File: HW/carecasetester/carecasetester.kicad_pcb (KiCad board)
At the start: 2 copper layers, 158.3 x 160.4 mm, 71 parts, among them J1 Conn_01x16_Female, J10-TP22 Conn_01x01_Male, J11-TP7 Conn_01x01_Male, J12-TP14 Conn_01x01_Male, J13-TP23 Conn_01x01_Male, J14-TP17 Conn_01x01_Male, J15 Conn_01x16_Male, J15-TP1 Conn_01x01_Male, J15-TP20 Conn_01x01_Male, J16-TP2 Conn_01x01_Male, J16-TP24 Conn_01x01_Male, J17-TP3 Conn_01x01_Male, J18-TP4 Conn_01x01_Male, J19-TP6 Conn_01x01_Male, J2 Conn_01x16_Female, J20-TP9 Conn_01x01_Male, J21-TP10 Conn_01x01_Male, J22-TP11 Conn_01x01_Male, J23-TP12 Conn_01x01_Male, J24-TP15 Conn_01x01_Male, J25-TP18 Conn_01x01_Male, J26-TP5 Conn_01x01_Male, J27-TP26 Conn_01x01_Male, J3 Conn_01x04_Female, J4 Conn_01x06_Male, J4-TP16 Conn_01x01_Male, J5 12V_Psu, J5-TP8 Conn_01x01_Male, J5-~E1 Conn_01x02_Male, J6-TP21 Conn_01x01_Male, J7-TP27 Conn_01x01_Male, J8-TP13 Conn_01x01_Male, J9-TP19 Conn_01x01_Male, K1 AZ952, Q1 BC847, SW1 SW_DIP_x02, U1 CD74HC4067M, U2 L7805

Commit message: missing schematic. (went poof)
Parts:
- added PulldownKnap: 4k7, Resistor_SMD:R_0603_1608Metric_Pad1.05x0.95mm_HandSolder, F.Cu at (208.8, 31.8)
- C1, C3: footprint Capacitor_SMD:C_0603_1608Metric_Pad1.05x0.95mm_HandSolder -> Capacitor_SMD:CP_Elec_6.3x5.4
- J5: moved to B.Cu
- moved R1 38.1 mm to (128.3, 47.4)
- moved J1 38.1 mm to (128.3, 52.3), turned to 270 degrees
- moved J2 38.1 mm to (167.3, 52.3), turned to 90 degrees
- moved D1 33.1 mm to (213.8, 54.0), turned to 90 degrees
- moved C1 19.1 mm to (157.0, 29.8), turned to 180 degrees
- moved C2 10.6 mm to (169.1, 33.0), turned to 180 degrees
- moved C3 9.85 mm to (181.7, 31.6), turned to 0 degrees
- turned J5 to 0 degrees
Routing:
- net Net-(J1-Pad3): track 189.6 -> 48.4 mm, vias 1 -> 0
- net Net-(J1-Pad4): track 185.5 -> 52.5 mm, vias 1 -> 0
- net Net-(J1-Pad5): track 180.3 -> 58.0 mm, vias 1 -> 0
- net Net-(J1-Pad6): track 175.7 -> 63.4 mm, vias 1 -> 0
- net Net-(J1-Pad7): track 171.0 -> 68.9 mm, vias 1 -> 0
- net Net-(J1-Pad8): track 163.7 -> 74.3 mm, vias 1 -> 0
- net Net-(J1-Pad9): track 157.5 -> 79.8 mm, vias 1 -> 0
- net Net-(J1-Pad10): track 151.5 -> 85.8 mm, vias 1 -> 0
- net Net-(J1-Pad11): track 143.3 -> 90.7 mm, vias 1 -> 0
- net Net-(D1-Pad1): track 157.8 -> 201.7 mm, vias 2 -> 4
- net Net-(J1-Pad12): track 138.4 -> 96.2 mm, vias 1 -> 0
- net Net-(J1-Pad13): track 129.5 -> 101.6 mm, vias 1 -> 0
- net Net-(J15-Pad6): track 140.5 -> 117.4 mm
- net Net-(J1-Pad14): track 122.0 -> 107.1 mm, vias 1 -> 0
- net Net-(J15-Pad10): track 119.7 -> 110.8 mm, vias 1 -> 3
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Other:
- outline, holes or cut-outs redrawn
- board text added: "1 2 3 4 5 6 7 8 9 10 11 12 13 14 15 16"
- board text added: "14 13 12 11 10 9 8 7 6 5 4 3 2 1 15 16"
- board text added: "C1+C2 footprints ændret til cp_elec 6.3-5.4 pulldown_knap tilføjet (47k resistor) byt ben i schematic på 12v stik (texas stik) Lav relay sheetet med Q1, R27 + D2"
- board text added: "Flip display headder"
- board text added: "GND TP1 TP2 TP3 TP4 TP6 TP9 TP10 TP11 TP12 TP15 TP18 TP5 TP26 GND GND"
- board text added: "SCL SDA +5V GND"

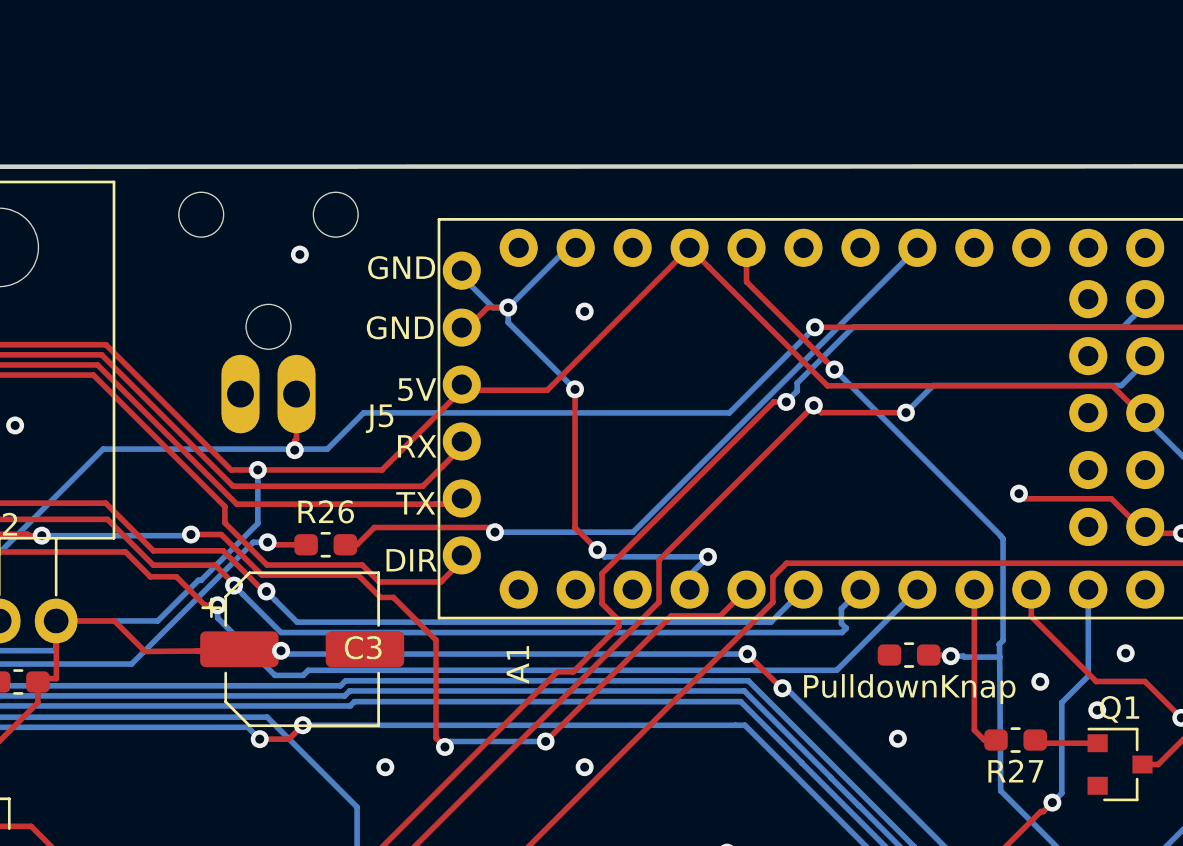
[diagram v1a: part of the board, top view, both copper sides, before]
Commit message: First try to fit schematic to pcb (not imported footprints to pcb yet)
Schematic: All known components has gotten an updated footprint
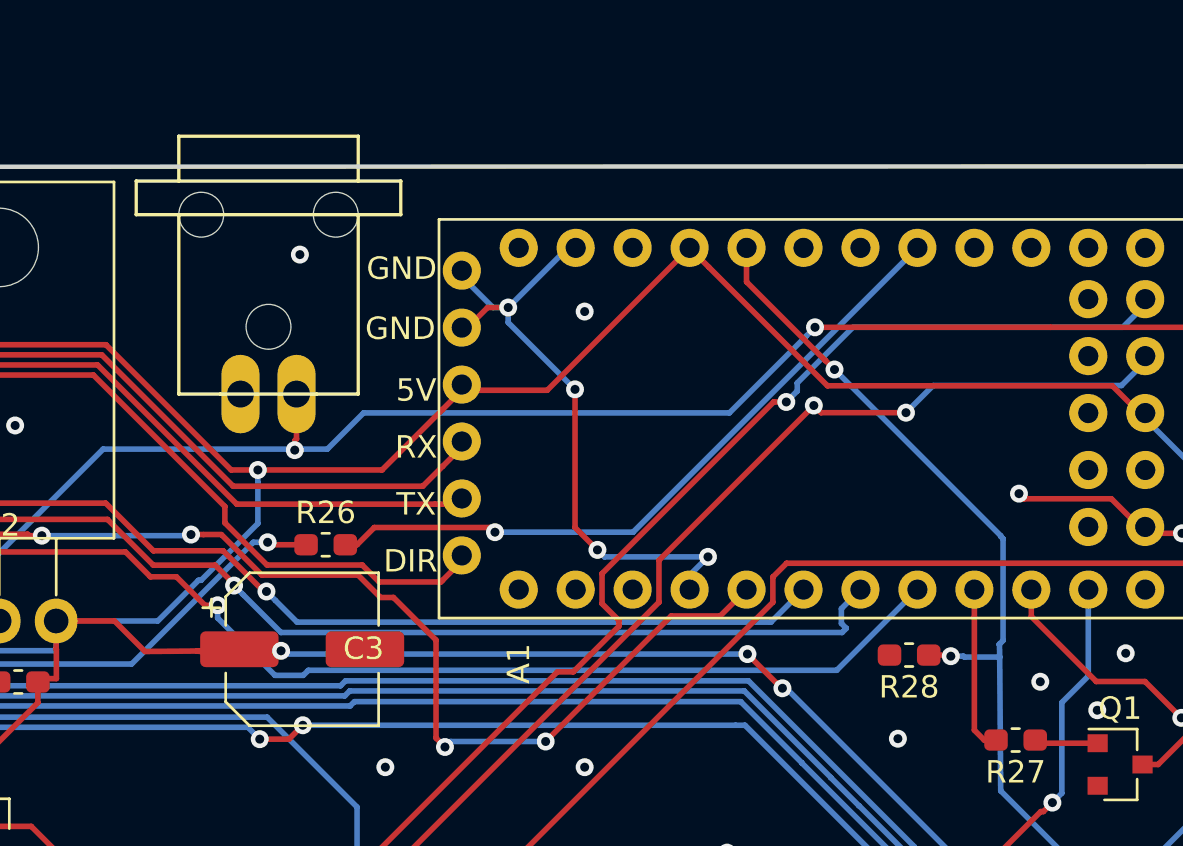
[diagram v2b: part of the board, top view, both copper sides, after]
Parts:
- J5: moved to F.Cu
- turned J5 to 180 degrees
- renumbered PulldownKnap to R28
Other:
- board text added: "C1+C3 footprints ændret til cp_elec 6.3-5.4 pulldown_knap tilføjet (47k resistor) byt ben i schematic på 12v stik (texas stik) Lav relay sheetet med Q1, R27 + D2"
- board text removed: "C1+C2 footprints ændret til cp_elec 6.3-5.4 pulldown_knap tilføjet (47k resistor) byt ben i schematic på 12v stik (texas stik) Lav relay sheetet med Q1, R27 + D2"

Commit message: PCB and Schematic are synced and gerbers can be made
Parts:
- Q1: value BC847 -> BC847W
- R28: value 4k7 -> 47k
- moved C3 0.54 mm to (181.2, 31.7)
- moved R28 0.32 mm to (208.5, 31.8), turned to 0 degrees
- moved C1 0.20 mm to (156.8, 29.8)
- moved D2 0.16 mm to (233.0, 31.0)
- moved Q1 0.08 mm to (218.3, 36.7)
- moved R27 0.08 mm to (213.6, 35.7)
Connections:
- net /RELAY/Relay_Driver renamed /RELAY/Relay_driver
- J5 pad 1: +12V -> GND
- J5 pad 2: GND -> +12V
- R28 pad 1: Net-(A1-Pad36) -> GND
- R28 pad 2: GND -> Net-(A1-Pad36)

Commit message: Fiksed silk front and back
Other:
- board size 158.3 x 160.4 mm -> 158.3 x 161.1 mm
- board text added: "DCTMM_CC-TESTER V0.2 02/04/2020"
- board text added: "GND CTS# +5V TXD RXD RTS#"
- board text added: "GND GND 5V RX TX DIR"
- board text added: "RAW GND RESET VCC A3 A2 A1 A0 13 12 11 10"
- board text added: "TXD RXD RESET GND 2 3 4 5 6 7 8 9"
- board text added: "~ET GND"
- board text removed: "DCTMM_CC-TESTER V0.1 20/02/2020"

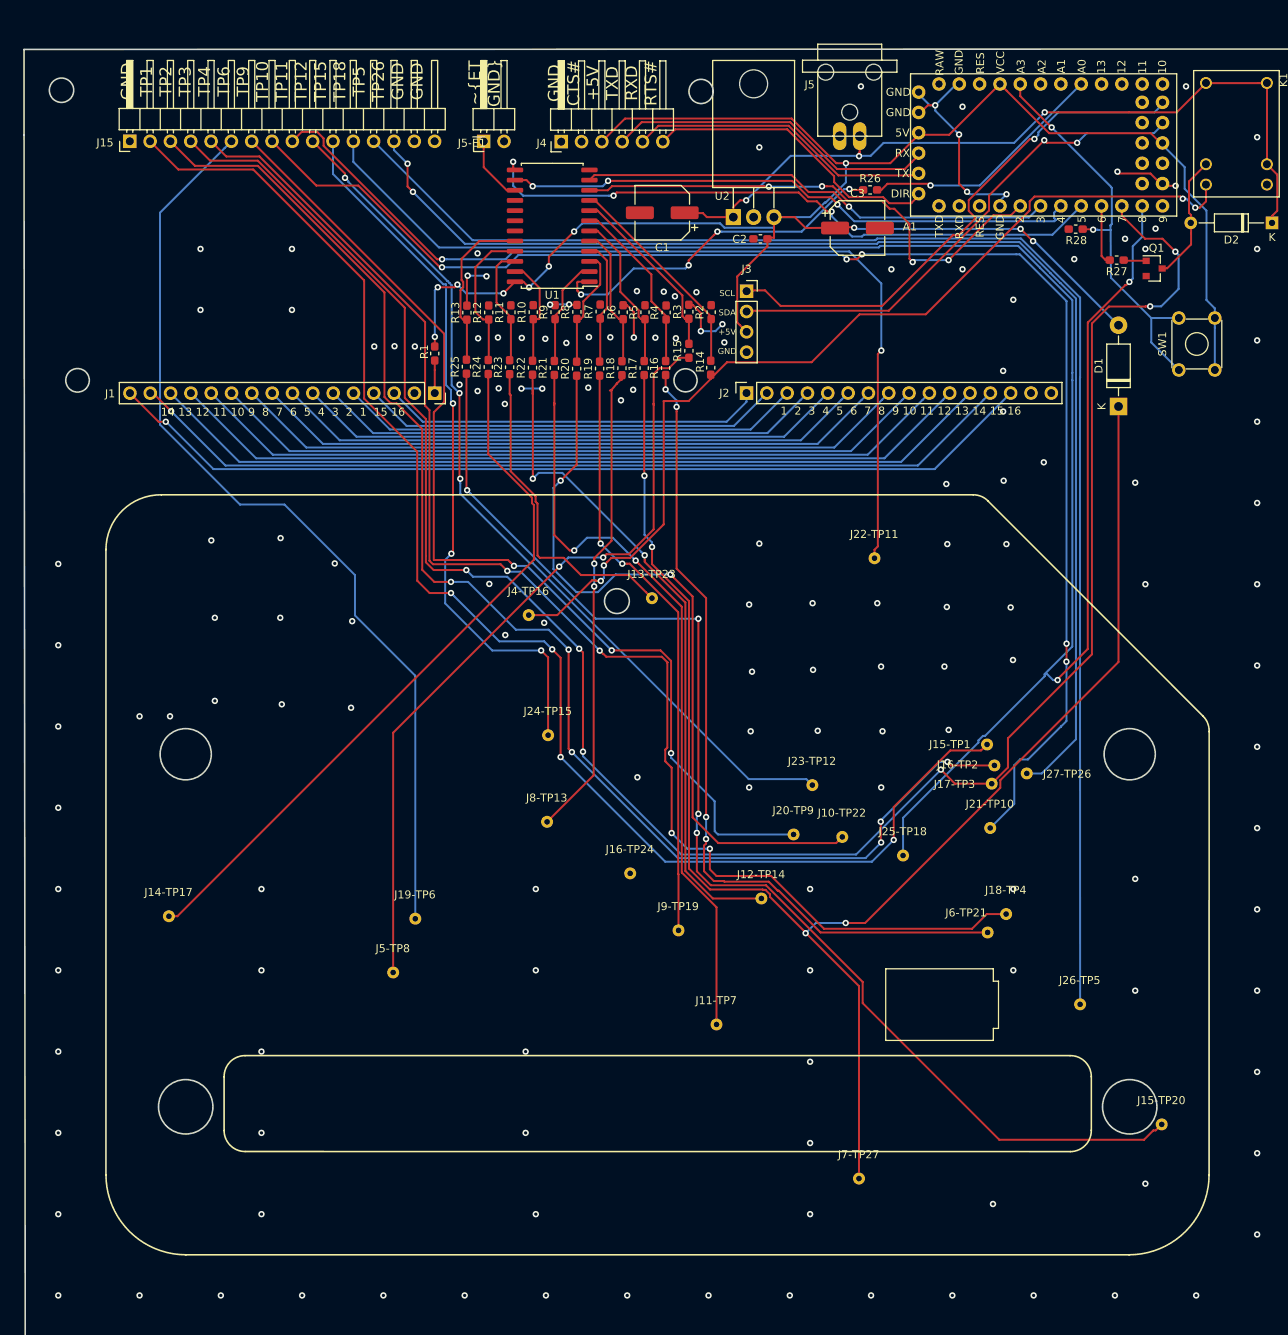
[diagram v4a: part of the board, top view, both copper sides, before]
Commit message: Gerbers and drillfiles made and ready to order
edge cuts file renamed to GML instaid of GM1
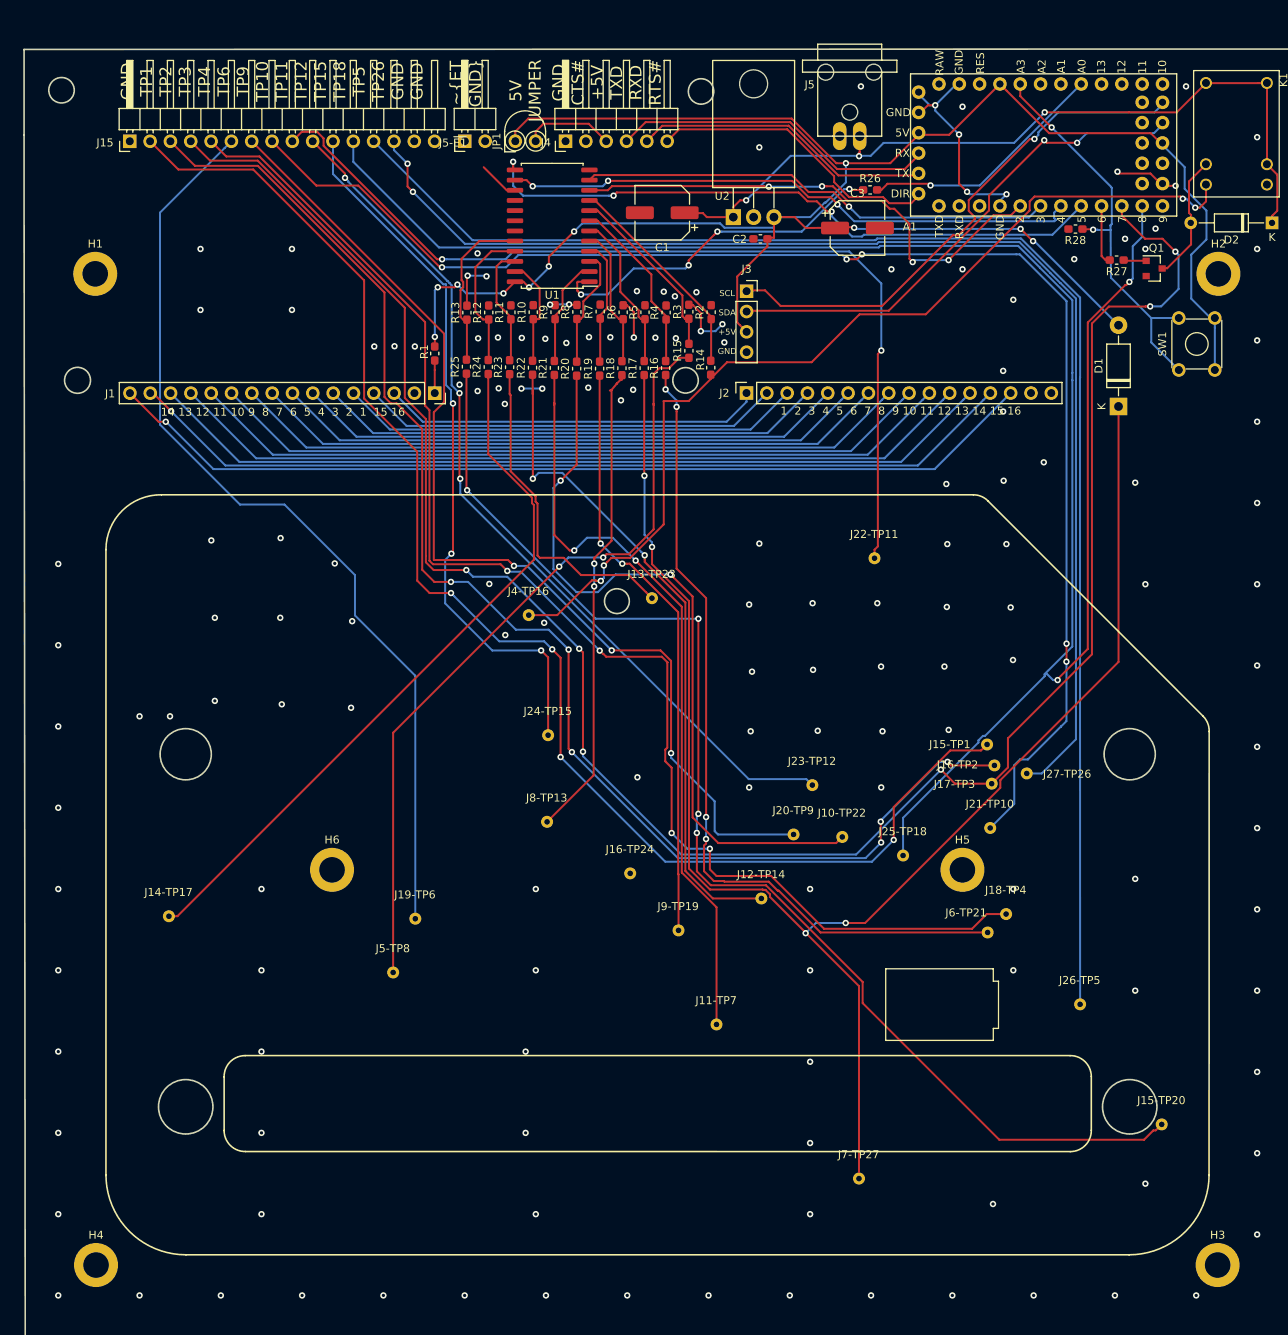
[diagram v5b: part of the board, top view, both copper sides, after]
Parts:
- added H1: MountingHole, MountingHole:MountingHole_3.2mm_M3_ISO14580_Pad, F.Cu at (85.9, 37.4)
- added H2: MountingHole, MountingHole:MountingHole_3.2mm_M3_ISO14580_Pad, F.Cu at (226.3, 37.4)
- added H3: MountingHole, MountingHole:MountingHole_3.2mm_M3_ISO14580_Pad, F.Cu at (226.2, 161.3)
- added H4: MountingHole, MountingHole:MountingHole_3.2mm_M3_ISO14580_Pad, F.Cu at (86.0, 161.3)
- added H5: MountingHole, MountingHole:MountingHole_3.2mm_M3_ISO14580_Pad, F.Cu at (194.3, 111.9)
- added H6: MountingHole, MountingHole:MountingHole_3.2mm_M3_ISO14580_Pad, F.Cu at (115.5, 111.9)
- added JP1: (NC), MM:Jumper_P2.54_Vertical_THT, F.Cu at (138.4, 20.8)
- moved J5-~E1 2.36 mm to (132.1, 20.8)
- moved J4 0.54 mm to (144.7, 20.8)
- turned R28 to 180 degrees
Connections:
- J4 pad 3: +5V -> Net-(J4-Pad3)
- R28 pad 1: GND -> Net-(A1-Pad36)
- R28 pad 2: Net-(A1-Pad36) -> GND
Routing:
- net +5V: track 247.6 -> 261.0 mm
- net Net-(J4-Pad3): track 0.00 -> 11.3 mm
- net Net-(J5-~E1-Pad1): track 8.34 -> 5.11 mm
- net Net-(A1-Pad3): track 37.3 -> 36.7 mm
- net Net-(A1-Pad17): track 37.9 -> 37.4 mm
- net Net-(A1-Pad15): track 41.2 -> 40.7 mm
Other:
- outline, holes or cut-outs redrawn
- board text added: "5V JUMPER"
- board text added: "DCTMM_CC-TESTER V0.2 03/04/2020"
- board text removed: "C1+C3 footprints ændret til cp_elec 6.3-5.4 pulldown_knap tilføjet (47k resistor) byt ben i schematic på 12v stik (texas stik) Lav relay sheetet med Q1, R27 + D2"
- board text removed: "DCTMM_CC-TESTER V0.2 02/04/2020"

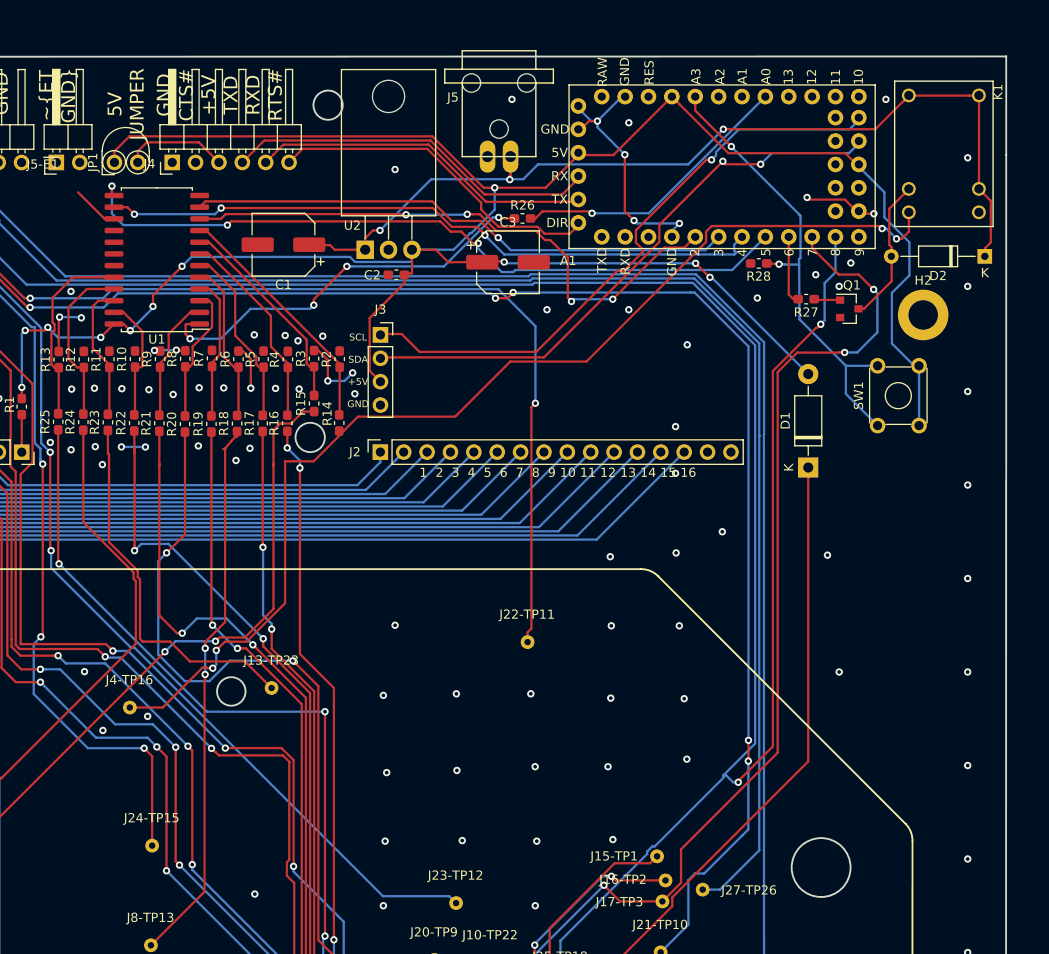
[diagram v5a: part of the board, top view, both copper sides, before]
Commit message: V0.22 gerbers
2nd relay added and all should now be ready to order
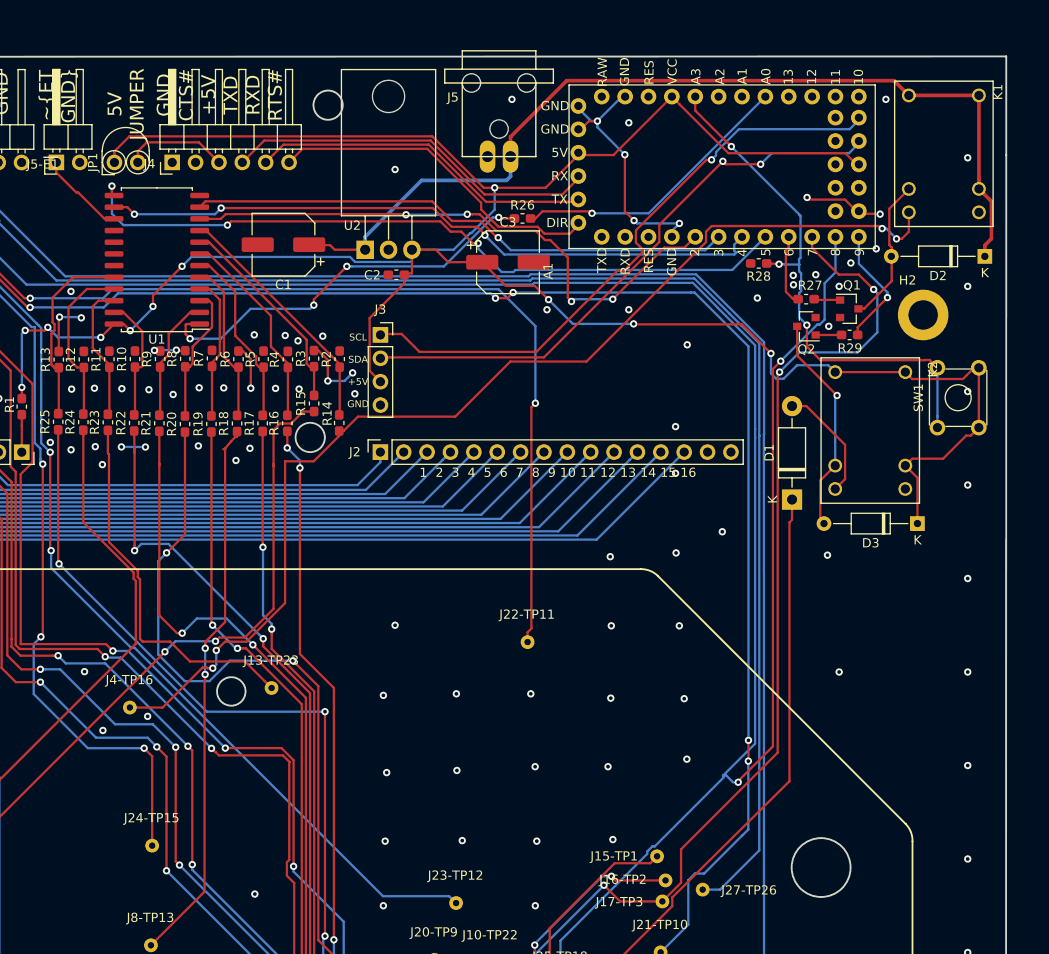
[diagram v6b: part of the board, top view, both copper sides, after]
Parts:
- added D3: 1N4148W, Diode_THT:D_DO-35_SOD27_P10.16mm_Horizontal, F.Cu at (225.7, 60.1)
- added K2: AZ952, athir:AZ952, F.Cu at (220.6, 50.0)
- added Q2: BC847W, Package_TO_SOT_SMD:SOT-23, F.Cu at (213.6, 38.6)
- added R29: 4k7, Resistor_SMD:R_0603_1608Metric_Pad1.05x0.95mm_HandSolder, F.Cu at (218.3, 39.6)
- moved SW1 6.50 mm to (227.8, 49.6)
- moved D1 3.90 mm to (212.1, 57.5)
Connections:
- net /4067/RELAY renamed /4067/RELAY12V
- net /RELAY/Relay_driver renamed /RELAY/Relay_driver1
- A1 pad 32: (no net) -> /RELAY/Relay_driver2
- D1 pad 2: +5V -> /4067/RELAYBAT
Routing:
- net Net-(D3-Pad2): track 0.00 -> 24.2 mm, vias 0 -> 1
- net /RELAY/Relay_driver2: track 0.00 -> 13.3 mm, vias 0 -> 1
- net /4067/RELAYBAT: track 0.00 -> 12.8 mm
- net +5V: track 261.0 -> 273.0 mm
- net Net-(A1-Pad36): track 50.8 -> 57.4 mm, vias 2 -> 3
- net Net-(J5-~E1-Pad1): track 5.11 -> 9.46 mm
- net Net-(D1-Pad1): track 201.7 -> 197.5 mm
- net Net-(Q2-Pad1): track 0.00 -> 2.82 mm
- net +12V: track 101.4 -> 102.8 mm, vias 3 -> 0
- net GND: vias 153 -> 157
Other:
- board text added: "DCTMM_CC-TESTER V0.21 06/04/2020"
- board text removed: "DCTMM_CC-TESTER V0.2 03/04/2020"
